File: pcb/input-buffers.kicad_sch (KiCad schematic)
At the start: 8 parts

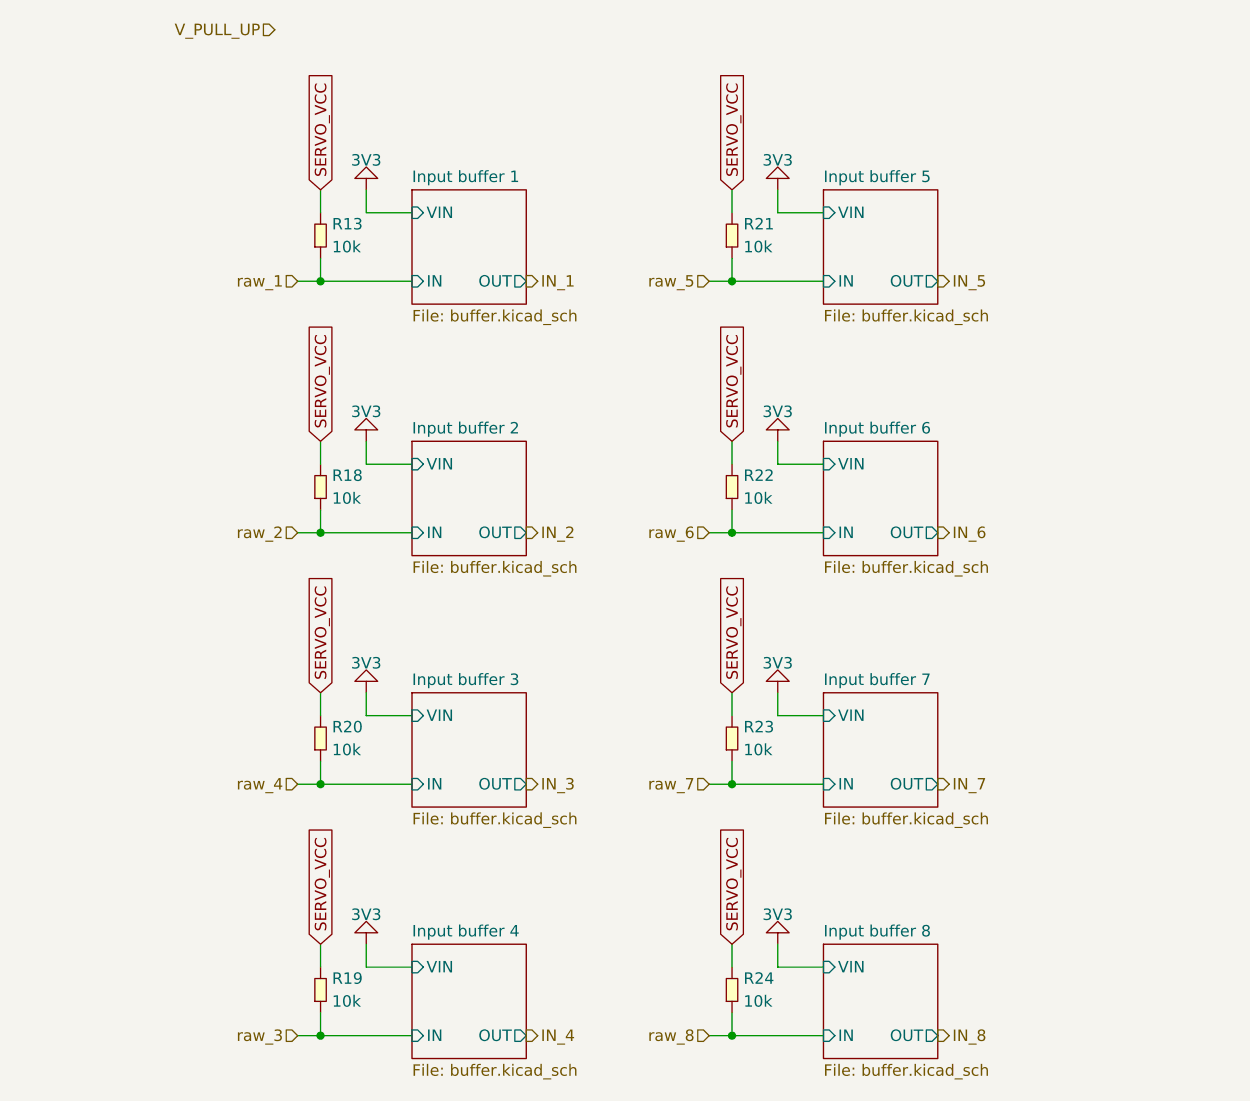
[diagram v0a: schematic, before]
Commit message: cleaned up buffer hierarchy
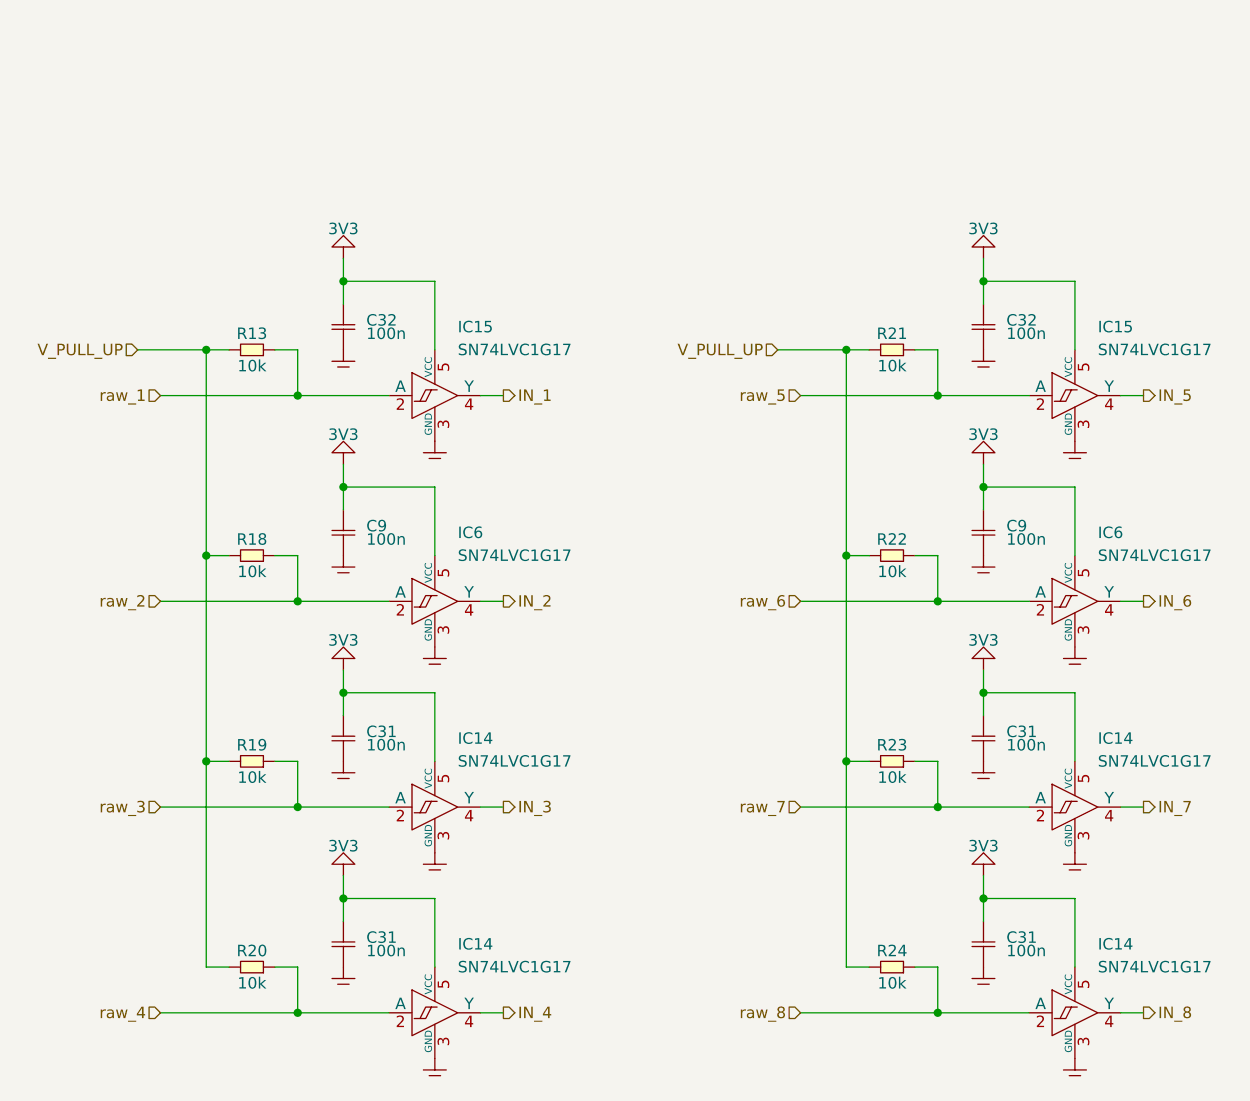
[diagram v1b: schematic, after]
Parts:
- added C31 (x4), C32 (x2), C9 (x2): 100n, SMT:0603, symbol generic:C
- added IC14 (x4), IC15 (x2), IC6 (x2): SN74LVC1G17, Single Schmitt-Trigger Buffer, symbol logic:SN74LVC1G17
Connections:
- net SERVO_VCC is gone; now on net V_PULL_UP: R13.2, R18.2, R19.2, R20.2, R21.2, R22.2, R23.2, R24.2
- net 3V3: now also C31.2, C31.2, C31.2, C31.2, C32.2, C32.2, C9.2, C9.2, IC14.5 (VCC), IC14.5 (VCC), IC14.5 (VCC), IC14.5 (VCC), IC15.5 (VCC), IC15.5 (VCC), IC6.5 (VCC), IC6.5 (VCC)
- net IN_1: now also IC15.4 (Y)
- net IN_2: now also IC6.4 (Y)
- net IN_3: now also IC14.4 (Y)
- net IN_4: now also IC14.4 (Y)
- net IN_5: now also IC15.4 (Y)
- net IN_6: now also IC6.4 (Y)
- net IN_7: now also IC14.4 (Y)
- net IN_8: now also IC14.4 (Y)
- net raw_1: now also IC15.2 (A)
- net raw_2: now also IC6.2 (A)
- net raw_3: now also IC14.2 (A)
- net raw_4: now also IC14.2 (A)
- net raw_5: now also IC15.2 (A)
- net raw_6: now also IC6.2 (A)
- net raw_7: now also IC14.2 (A)
- net raw_8: now also IC14.2 (A)
- new net GND: C31.1, C31.1, C31.1, C31.1, C32.1, C32.1, C9.1, C9.1, IC14.3 (GND), IC14.3 (GND), IC14.3 (GND), IC14.3 (GND), IC15.3 (GND), IC15.3 (GND), IC6.3 (GND), IC6.3 (GND)
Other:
- removed sheet Input buffer 1
- removed sheet Input buffer 2
- removed sheet Input buffer 3
- removed sheet Input buffer 4
- removed sheet Input buffer 5
- removed sheet Input buffer 6
- removed sheet Input buffer 7
- removed sheet Input buffer 8
- moved on the sheet: R13

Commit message: added power switch for servos
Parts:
- IC10, IC6: renamed from IC15; footprint Single Schmitt-Trigger Buffer -> sc70:SC70-5L
- IC11, IC7: renamed from IC6; footprint Single Schmitt-Trigger Buffer -> sc70:SC70-5L
- IC12, IC13, IC8, IC9: renamed from IC14; footprint Single Schmitt-Trigger Buffer -> sc70:SC70-5L
- renumbered C9 to C16, C31 to C17, C31 to C18, C32 to C19, C9 to C26, C31 to C27, C31 to C28, C32 to C9

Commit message: worked on layout
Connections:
- net IN_1: now also IC13.4 (Y); no longer IC6.4 (Y)
- net IN_2: now also IC12.4 (Y); no longer IC7.4 (Y)
- net IN_3: now also IC11.4 (Y); no longer IC8.4 (Y)
- net IN_4: now also IC10.4 (Y); no longer IC9.4 (Y)
- net IN_5: now also IC9.4 (Y); no longer IC10.4 (Y)
- net IN_6: now also IC8.4 (Y); no longer IC11.4 (Y)
- net IN_7: now also IC7.4 (Y); no longer IC12.4 (Y)
- net IN_8: now also IC6.4 (Y); no longer IC13.4 (Y)
- net raw_1: now also IC13.2 (A), R24.1; no longer IC6.2 (A), R13.1
- net raw_2: now also IC12.2 (A), R23.1; no longer IC7.2 (A), R18.1
- net raw_3: now also IC11.2 (A), R22.1; no longer IC8.2 (A), R19.1
- net raw_4: now also IC10.2 (A), R21.1; no longer IC9.2 (A), R20.1
- net raw_5: now also IC9.2 (A), R20.1; no longer IC10.2 (A), R21.1
- net raw_6: now also IC8.2 (A), R19.1; no longer IC11.2 (A), R22.1
- net raw_7: now also IC7.2 (A), R18.1; no longer IC12.2 (A), R23.1
- net raw_8: now also IC6.2 (A), R13.1; no longer IC13.2 (A), R24.1
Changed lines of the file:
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@@
 		)
 	)
-	(hierarchical_label "IN_7"
+	(hierarchical_label "IN_2"
 		(shape output)
 		(at 210.82 116.84 0)
@@
 		)
 	)
-	(hierarchical_label "raw_5"
+	(hierarchical_label "raw_4"
 		(shape input)
 		(at 172.72 71.12 180)
@@
 		)
 	)
-	(hierarchical_label "raw_8"
+	(hierarchical_label "raw_1"
 		(shape input)
 		(at 172.72 139.7 180)
@@
 		)
 	)
-	(hierarchical_label "IN_5"
+	(hierarchical_label "IN_4"
 		(shape output)
 		(at 210.82 71.12 0)
@@
 		)
 	)
-	(hierarchical_label "IN_3"
+	(hierarchical_label "IN_6"
 		(shape output)
 		(at 139.7 116.84 0)
@@
 		)
 	)
-	(hierarchical_label "raw_3"
+	(hierarchical_label "raw_6"
 		(shape input)
 		(at 101.6 116.84 180)
@@
 		)
 	)
-	(hierarchical_label "raw_1"
+	(hierarchical_label "raw_8"
 		(shape input)
 		(at 101.6 71.12 180)
@@
 		)
 	)
-	(hierarchical_label "raw_4"
+	(hierarchical_label "raw_5"
 		(shape input)
 		(at 101.6 139.7 180)
@@
 		)
 	)
-	(hierarchical_label "raw_7"
+	(hierarchical_label "raw_2"
 		(shape input)
 		(at 172.72 116.84 180)
@@
 		)
 	)
-	(hierarchical_label "IN_4"
+	(hierarchical_label "IN_5"
 		(shape output)
 		(at 139.7 139.7 0)
@@
 		)
 	)
-	(hierarchical_label "IN_2"
+	(hierarchical_label "IN_7"
 		(shape output)
 		(at 139.7 93.98 0)
@@
 		)
 	)
-	(hierarchical_label "IN_8"
+	(hierarchical_label "IN_1"
 		(shape output)
 		(at 210.82 139.7 0)
@@
 		)
 	)
-	(hierarchical_label "raw_2"
+	(hierarchical_label "raw_7"
 		(shape input)
 		(at 101.6 93.98 180)
@@
 		)
 	)
-	(hierarchical_label "IN_6"
+	(hierarchical_label "IN_3"
 		(shape output)
 		(at 210.82 93.98 0)
@@
 		)
 	)
-	(hierarchical_label "raw_6"
+	(hierarchical_label "raw_3"
 		(shape input)
 		(at 172.72 93.98 180)
@@
 		)
 	)
-	(hierarchical_label "IN_1"
+	(hierarchical_label "IN_8"
 		(shape output)
 		(at 139.7 71.12 0)
